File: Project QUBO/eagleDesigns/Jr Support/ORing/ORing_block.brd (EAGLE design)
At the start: 152.4 x 101.6 mm, 73 parts

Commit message: 
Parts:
- moved U$6 139.5 mm to (84.3, 14.4), turned to 180 degrees
- moved R21 116.1 mm to (41.1, 22.3), turned to 180 degrees
- moved U$57 115.7 mm to (75.9, 93.9), turned to 180 degrees
- moved R20 110.3 mm to (41.0, 25.5)
- moved C64 106.2 mm to (29.6, 22.3)
- moved U$1 104.5 mm to (-34.3, 38.1), turned to 180 degrees
- moved AUDIO1 103.0 mm to (39.7, 41.8), turned to 90 degrees
- moved JP6 102.9 mm to (82.9, 7.28)
- moved R27 97.2 mm to (41.1, 28.6), turned to 180 degrees
- moved R15 94.2 mm to (32.0, 53.6), turned to 90 degrees
- moved LED2 93.5 mm to (32.1, 40.1), turned to 180 degrees
- moved R17 93.0 mm to (32.0, 49.1), turned to 90 degrees
- moved U$56 92.8 mm to (77.0, 86.6)
- moved R16 88.2 mm to (32.0, 44.5), turned to 90 degrees
- moved LED3 87.3 mm to (23.2, 54.0), turned to 180 degrees
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
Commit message: 
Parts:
- moved TEST-PTS1 130.5 mm to (48.6, 82.6), turned to 180 degrees
- moved U$12 91.2 mm to (42.4, 83.0), turned to 90 degrees
- moved POT1 87.0 mm to (47.4, 87.4)
- moved R31 81.8 mm to (42.4, 78.7)
- moved LED6 62.4 mm to (39.2, 82.6), turned to 90 degrees
- moved R20 39.5 mm to (7.32, 46.1), turned to 180 degrees
- moved R27 39.1 mm to (7.37, 48.5), turned to 0 degrees
- moved R26 38.6 mm to (8.58, 61.4)
- moved R21 37.9 mm to (11.6, 46.1)
- moved R24 37.5 mm to (21.6, 46.4)
- moved R22 37.4 mm to (15.9, 46.1)
- moved R28 37.3 mm to (21.5, 56.4)
- moved R23 37.2 mm to (21.5, 51.2)
- moved C64 36.0 mm to (18.1, 56.4), turned to 90 degrees
- moved U$27 34.3 mm to (13.0, 56.1), turned to 180 degrees
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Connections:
- new net N$28: R30.1, U$1.ENOUT, U$10.1
- new net N$29: R19.1, U$27.ENOUT, U$9.1
- net V_BATT1: no longer R19.1, U$27.ENOUT, U$9.1
- net V_BATT2: no longer R30.1, U$10.1

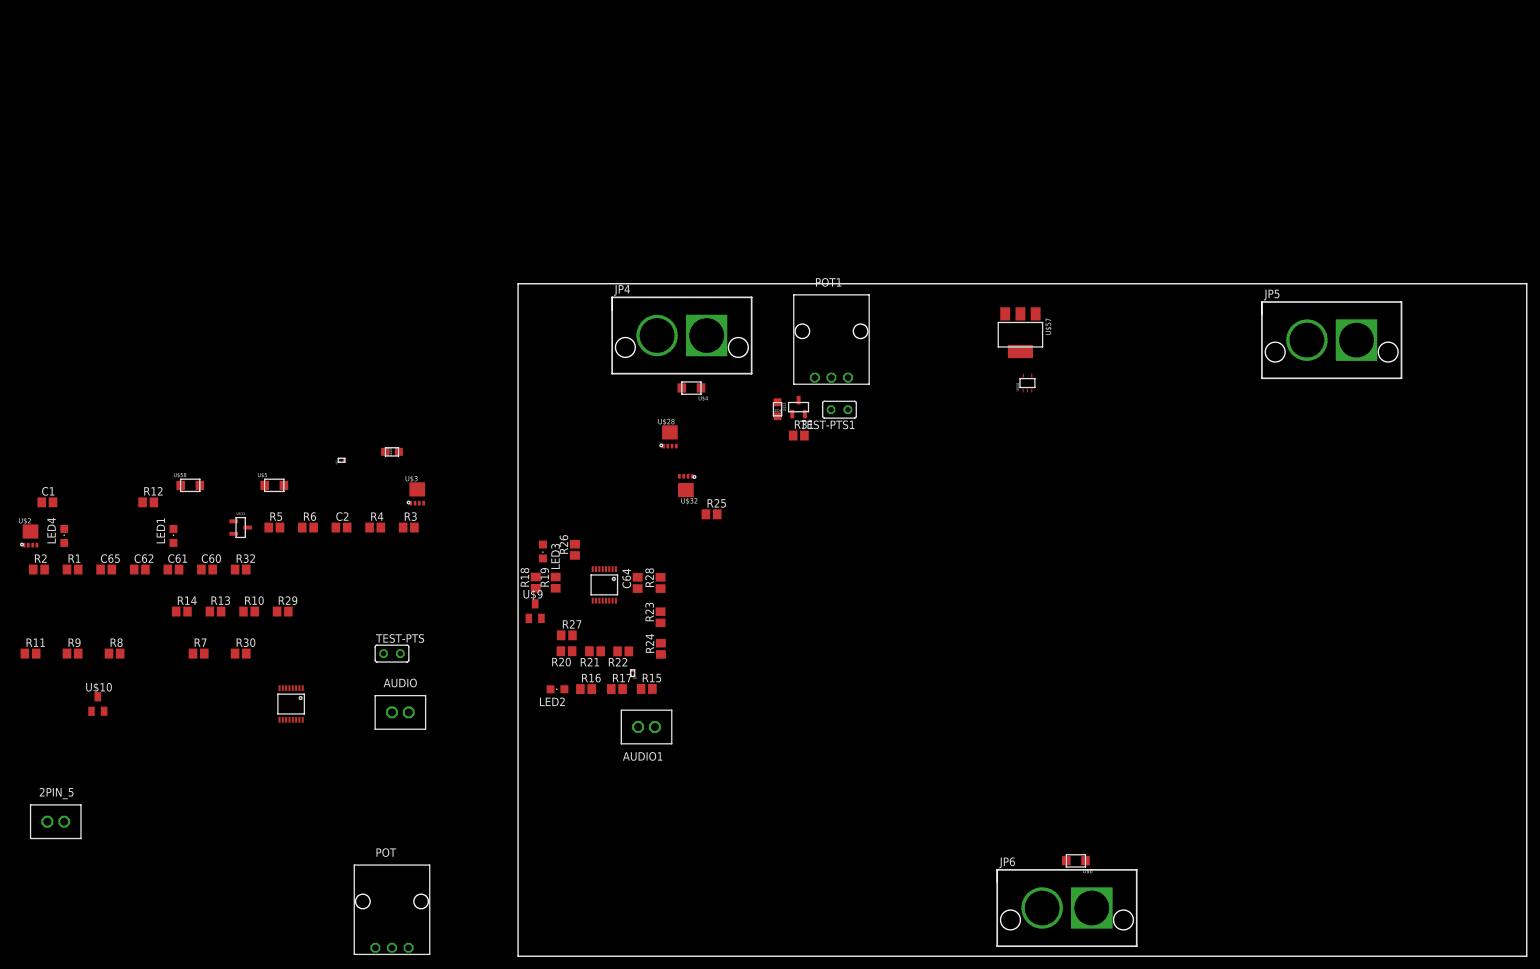
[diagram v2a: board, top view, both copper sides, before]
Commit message: 
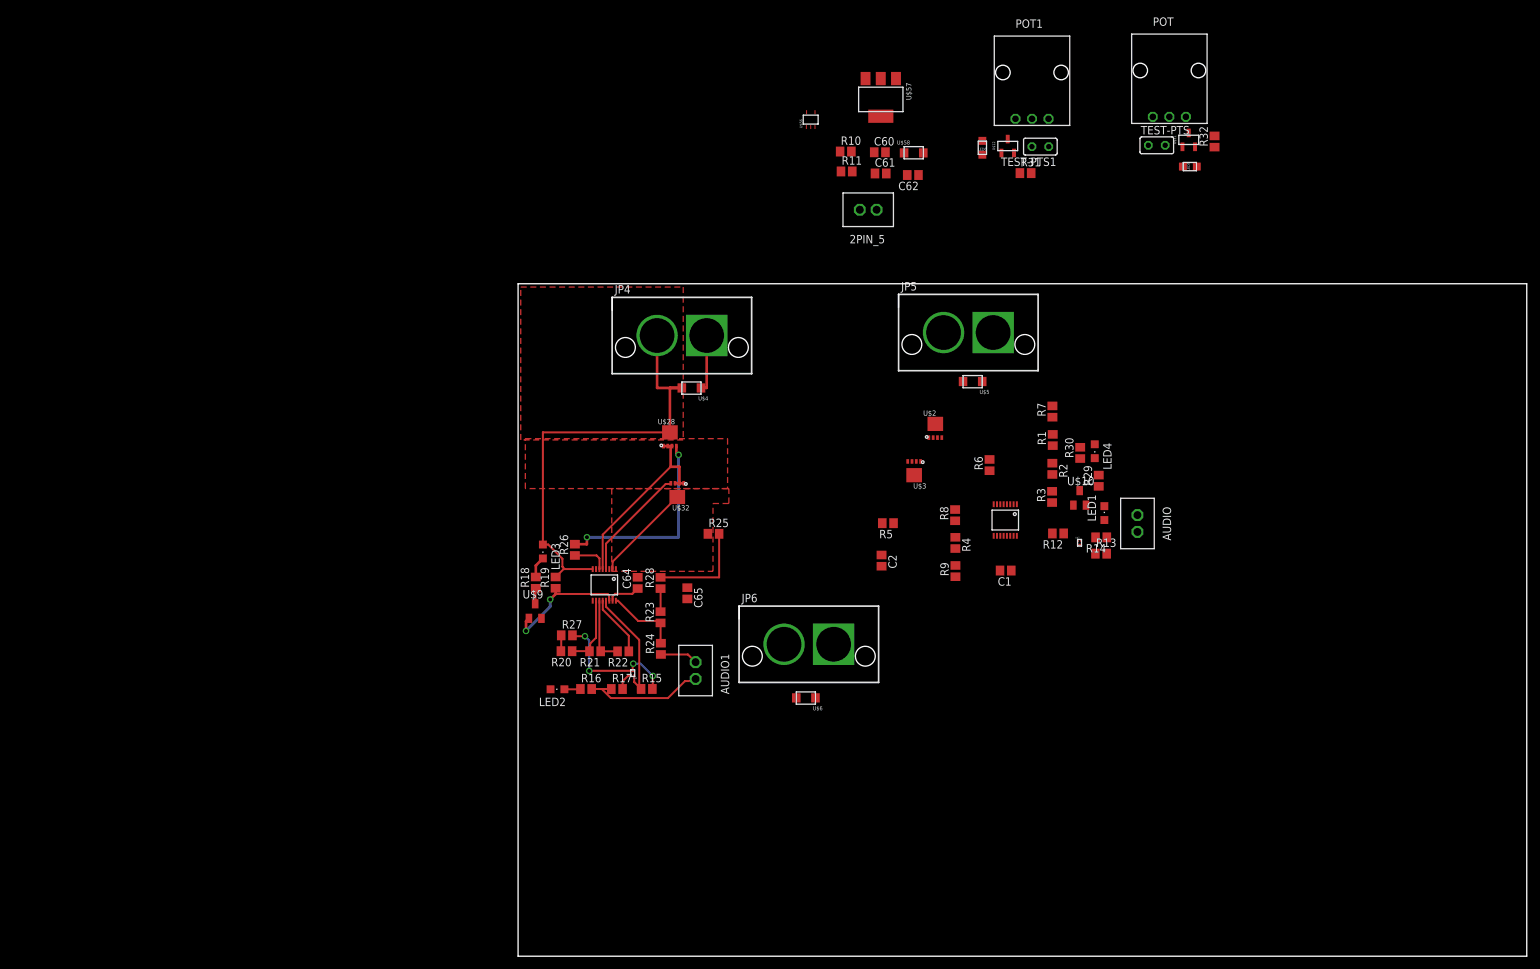
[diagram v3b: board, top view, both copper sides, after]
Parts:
- moved POT 171.9 mm to (98.4, 126.8)
- moved R32 160.7 mm to (105.2, 123.1), turned to 90 degrees
- moved LED4 156.2 mm to (87.1, 76.3), turned to 180 degrees
- moved U$11 154.8 mm to (101.3, 123.3), turned to 90 degrees
- moved R2 153.9 mm to (80.7, 73.6), turned to 270 degrees
- moved 2PIN_5 153.7 mm to (52.9, 112.8), turned to 180 degrees
- moved U$10 151.6 mm to (84.8, 69.2)
- moved R1 149.4 mm to (80.8, 78.0), turned to 90 degrees
- moved C1 145.2 mm to (73.7, 58.3), turned to 180 degrees
- moved R11 143.2 mm to (49.6, 118.6)
- moved LED1 140.7 mm to (88.6, 67.0)
- moved R14 139.4 mm to (88.1, 63.3), turned to 180 degrees
- moved TEST-PTS 138.7 mm to (96.5, 122.5)
- moved U$2 137.7 mm to (63.0, 79.8)
- moved R12 137.5 mm to (81.6, 63.9), turned to 180 degrees
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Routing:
- net V_BATT1: track 0.00 -> 88.8 mm, vias 0 -> 4
- net N$59: track 0.00 -> 30.8 mm, vias 0 -> 2
- net N$54: track 0.00 -> 29.5 mm
- net GND: track 0.00 -> 23.8 mm
- net N$29: track 0.00 -> 19.3 mm, vias 0 -> 2
- net N$22: track 0.00 -> 19.1 mm
- net N$20: track 0.00 -> 18.0 mm
- net N$61: track 0.00 -> 17.4 mm
- net V_BATT: track 0.00 -> 15.4 mm
- net N$60: track 0.00 -> 14.9 mm
- net N$50: track 0.00 -> 11.2 mm
- net N$39: track 0.00 -> 10.7 mm
- net N$47: track 0.00 -> 10.3 mm
- net N$37: track 0.00 -> 5.52 mm
- net N$53: track 0.00 -> 4.94 mm
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- added copper zone on layer 1, net N$54
- added copper zone on layer 1, net N$60
- added copper zone on layer 1, net V_BATT1
